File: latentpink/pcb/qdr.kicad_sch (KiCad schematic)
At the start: 69 parts, among them U2 XC7K160T-2FBG484C, U28 IS25WP256D-JLLE, U29 DSC1123CI2-150.0000T, U3 CY7C2245KV18-450BZXI

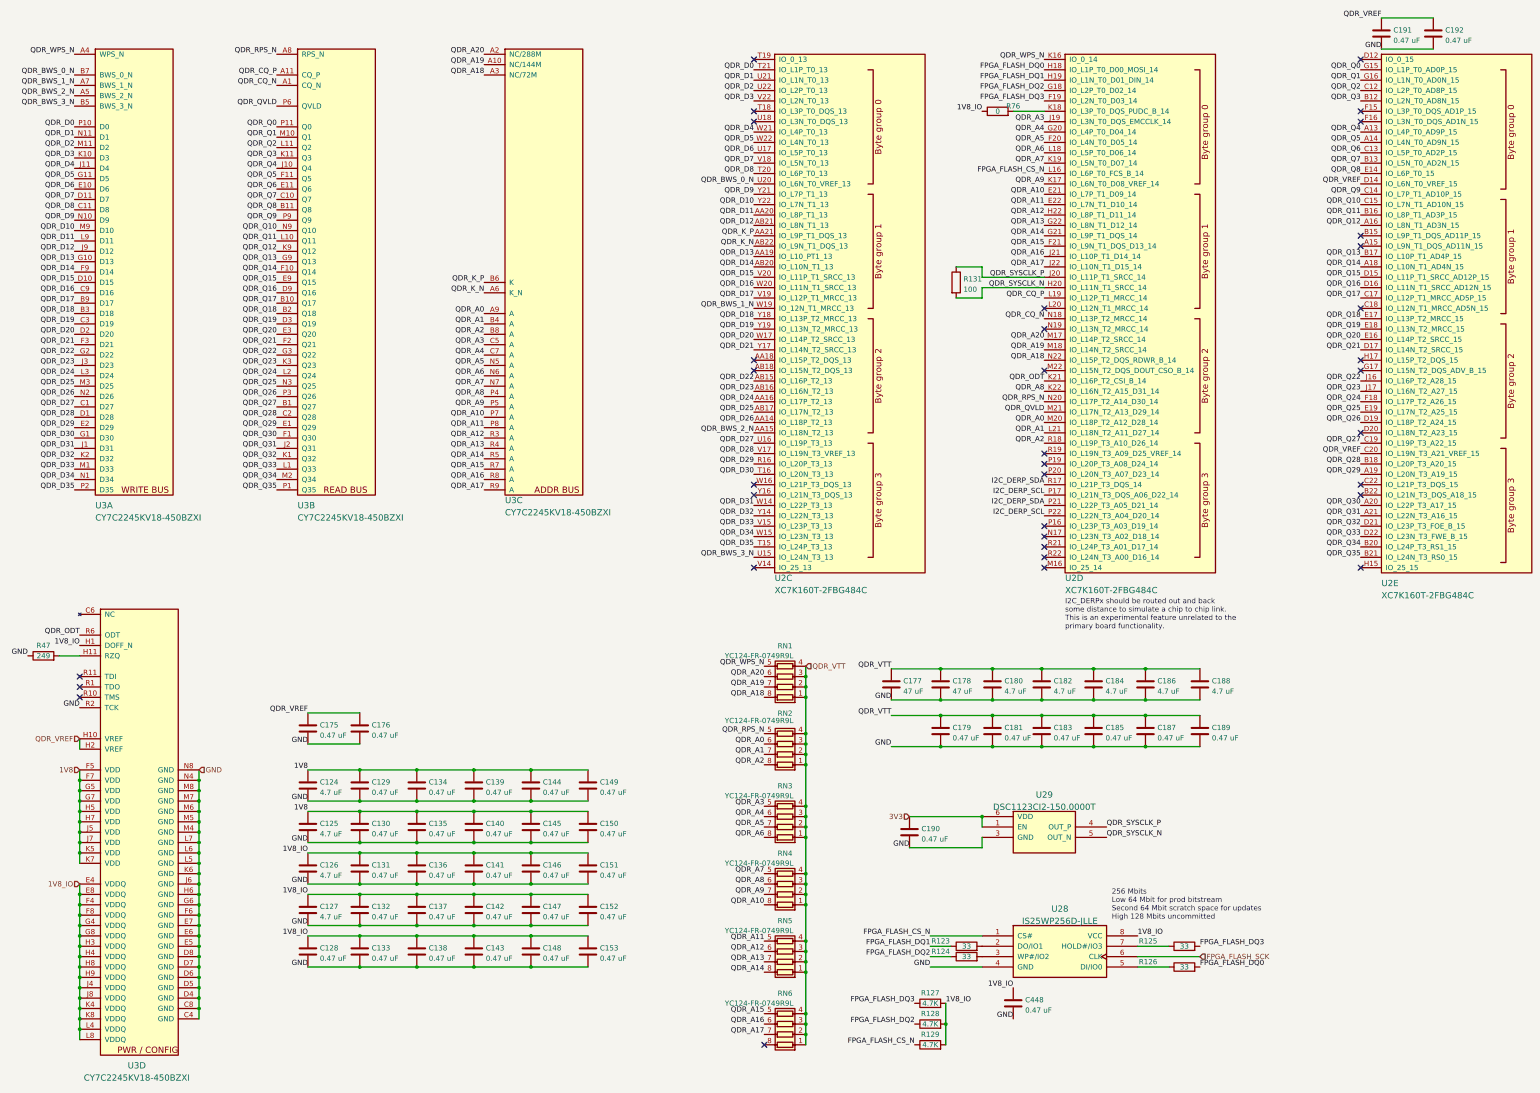
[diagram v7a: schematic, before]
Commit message: Began QDR layout
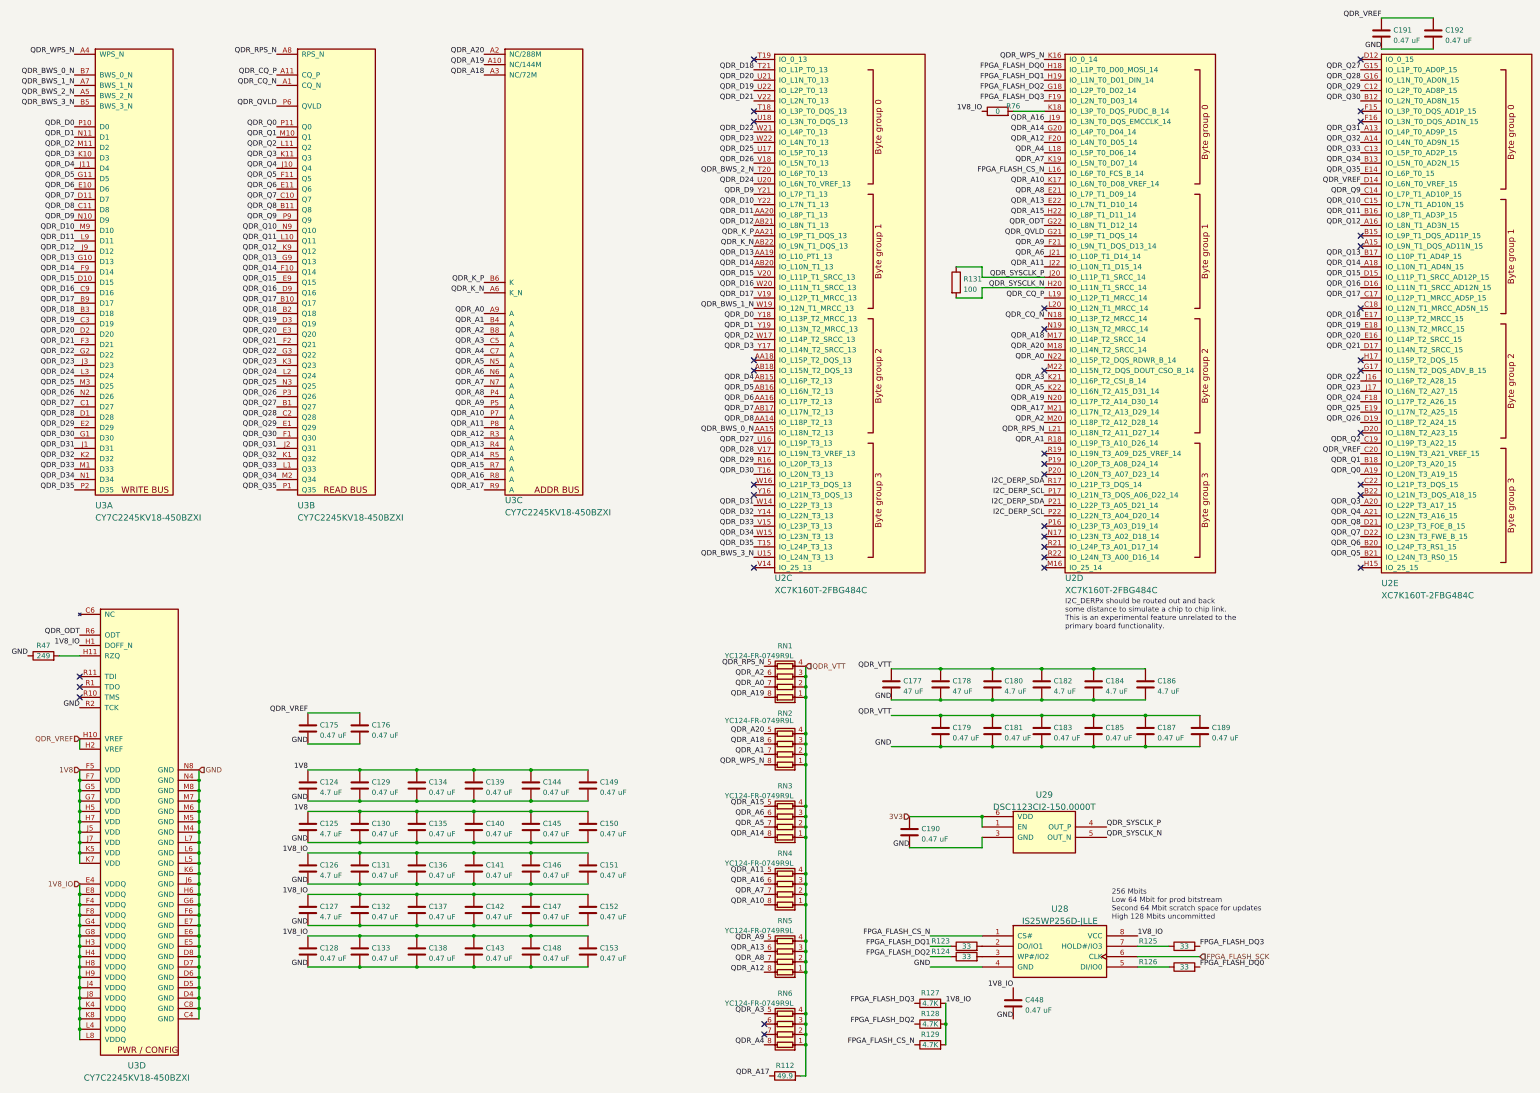
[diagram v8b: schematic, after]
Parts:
- removed C188: 4.7 uF, azonenberg_pcb:EIA_0603_CAP_NOSILK, symbol device:C
- added R112: 49.9, azonenberg_pcb:EIA_0402_RES_NOSILK, symbol device:R
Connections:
- net QDR_A0: now also RN1.7 (R2.2), U2.N22 (IO_L15P_T2_DQS_RDWR_B_14); no longer RN2.6 (R3.2), U2.M20 (IO_L18P_T2_A12_D28_14)
- net QDR_A1: now also U2.R18 (IO_L19P_T3_A10_D26_14); no longer U2.L21 (IO_L18N_T2_A11_D27_14)
- net QDR_A10: now also U2.K17 (IO_L6N_T0_D08_VREF_14); no longer U2.E21 (IO_L7P_T1_D09_14)
- net QDR_A11: now also RN4.5 (R4.2), U2.J22 (IO_L10N_T1_D15_14); no longer RN5.5 (R4.2), U2.E22 (IO_L7N_T1_D10_14)
- net QDR_A12: now also RN5.8 (R1.2), U2.F20 (IO_L4N_T0_D05_14); no longer RN5.6 (R3.2), U2.H22 (IO_L8P_T1_D11_14)
- net QDR_A13: now also RN5.6 (R3.2), U2.E22 (IO_L7N_T1_D10_14); no longer RN5.7 (R2.2), U2.G22 (IO_L8N_T1_D12_14)
- net QDR_A14: now also RN3.8 (R1.2), U2.G20 (IO_L4P_T0_D04_14); no longer RN5.8 (R1.2), U2.G21 (IO_L9P_T1_DQS_14)
- net QDR_A15: now also RN3.5 (R4.2), U2.H22 (IO_L8P_T1_D11_14); no longer RN6.5 (R4.2), U2.F21 (IO_L9N_T1_DQS_D13_14)
- net QDR_A16: now also RN4.6 (R3.2), U2.J19 (IO_L3N_T0_DQS_EMCCLK_14); no longer RN6.6 (R3.2), U2.J21 (IO_L10P_T1_D14_14)
- net QDR_A17: now also U2.M21 (IO_L17N_T2_A13_D29_14), R112.1; no longer RN6.7 (R2.2), U2.J22 (IO_L10N_T1_D15_14)
- net QDR_A18: now also RN2.6 (R3.2), U2.M17 (IO_L14P_T2_SRCC_14); no longer RN1.8 (R1.2), U2.N22 (IO_L15P_T2_DQS_RDWR_B_14)
- net QDR_A19: now also RN1.8 (R1.2), U2.N20 (IO_L17P_T2_A14_D30_14); no longer RN1.7 (R2.2), U2.M18 (IO_L14N_T2_SRCC_14)
- net QDR_A2: now also RN1.6 (R3.2), U2.M20 (IO_L18P_T2_A12_D28_14); no longer RN2.8 (R1.2), U2.R18 (IO_L19P_T3_A10_D26_14)
- net QDR_A20: now also RN2.5 (R4.2), U2.M18 (IO_L14N_T2_SRCC_14); no longer RN1.6 (R3.2), U2.M17 (IO_L14P_T2_SRCC_14)
- net QDR_A3: now also RN6.5 (R4.2), U2.K21 (IO_L16P_T2_CSI_B_14); no longer RN3.5 (R4.2), U2.J19 (IO_L3N_T0_DQS_EMCCLK_14)
- net QDR_A4: now also RN6.8 (R1.2), U2.L18 (IO_L5P_T0_D06_14); no longer RN3.6 (R3.2), U2.G20 (IO_L4P_T0_D04_14)
- net QDR_A5: now also U2.K22 (IO_L16N_T2_A15_D31_14); no longer U2.F20 (IO_L4N_T0_D05_14)
- net QDR_A6: now also RN3.6 (R3.2), U2.J21 (IO_L10P_T1_D14_14); no longer RN3.8 (R1.2), U2.L18 (IO_L5P_T0_D06_14)
- net QDR_A7: now also RN4.7 (R2.2); no longer RN4.5 (R4.2)
- net QDR_A8: now also RN5.7 (R2.2), U2.E21 (IO_L7P_T1_D09_14); no longer RN4.6 (R3.2), U2.K22 (IO_L16N_T2_A15_D31_14)
- net QDR_A9: now also RN5.5 (R4.2), U2.F21 (IO_L9N_T1_DQS_D13_14); no longer RN4.7 (R2.2), U2.K17 (IO_L6N_T0_D08_VREF_14)
- net QDR_BWS_0_N: now also U2.AA15 (IO_L18N_T2_13); no longer U2.U20 (IO_L6N_T0_VREF_13)
- net QDR_BWS_2_N: now also U2.T20 (IO_L6P_T0_13); no longer U2.AA15 (IO_L18N_T2_13)
- net QDR_D0: now also U2.Y18 (IO_L13P_T2_MRCC_13); no longer U2.T21 (IO_L1P_T0_13)
- net QDR_D1: now also U2.Y19 (IO_L13N_T2_MRCC_13); no longer U2.U21 (IO_L1N_T0_13)
- net QDR_D18: now also U2.T21 (IO_L1P_T0_13); no longer U2.Y18 (IO_L13P_T2_MRCC_13)
- net QDR_D19: now also U2.U22 (IO_L2P_T0_13); no longer U2.Y19 (IO_L13N_T2_MRCC_13)
- net QDR_D2: now also U2.W17 (IO_L14P_T2_SRCC_13); no longer U2.U22 (IO_L2P_T0_13)
- net QDR_D20: now also U2.U21 (IO_L1N_T0_13); no longer U2.W17 (IO_L14P_T2_SRCC_13)
- net QDR_D21: now also U2.V22 (IO_L2N_T0_13); no longer U2.Y17 (IO_L14N_T2_SRCC_13)
- net QDR_D22: now also U2.W21 (IO_L4P_T0_13); no longer U2.AB15 (IO_L16P_T2_13)
- net QDR_D23: now also U2.W22 (IO_L4N_T0_13); no longer U2.AB16 (IO_L16N_T2_13)
- net QDR_D24: now also U2.U20 (IO_L6N_T0_VREF_13); no longer U2.AA16 (IO_L17P_T2_13)
- net QDR_D25: now also U2.U17 (IO_L5P_T0_13); no longer U2.AB17 (IO_L17N_T2_13)
- net QDR_D26: now also U2.V18 (IO_L5N_T0_13); no longer U2.AA14 (IO_L18P_T2_13)
- net QDR_D3: now also U2.Y17 (IO_L14N_T2_SRCC_13); no longer U2.V22 (IO_L2N_T0_13)
- net QDR_D4: now also U2.AB15 (IO_L16P_T2_13); no longer U2.W21 (IO_L4P_T0_13)
- net QDR_D5: now also U2.AB16 (IO_L16N_T2_13); no longer U2.W22 (IO_L4N_T0_13)
- net QDR_D6: now also U2.AA16 (IO_L17P_T2_13); no longer U2.U17 (IO_L5P_T0_13)
- net QDR_D7: now also U2.AB17 (IO_L17N_T2_13); no longer U2.V18 (IO_L5N_T0_13)
- net QDR_D8: now also U2.AA14 (IO_L18P_T2_13); no longer U2.T20 (IO_L6P_T0_13)
- net QDR_ODT: now also U2.G22 (IO_L8N_T1_D12_14); no longer U2.K21 (IO_L16P_T2_CSI_B_14)
- net QDR_Q0: now also U2.A19 (IO_L20N_T3_A19_15); no longer U2.G15 (IO_L1P_T0_AD0P_15)
- net QDR_Q1: now also U2.B18 (IO_L20P_T3_A20_15); no longer U2.G16 (IO_L1N_T0_AD0N_15)
- net QDR_Q2: now also U2.C19 (IO_L19P_T3_A22_15); no longer U2.C12 (IO_L2P_T0_AD8P_15)
- net QDR_Q27: now also U2.G15 (IO_L1P_T0_AD0P_15); no longer U2.C19 (IO_L19P_T3_A22_15)
- net QDR_Q28: now also U2.G16 (IO_L1N_T0_AD0N_15); no longer U2.B18 (IO_L20P_T3_A20_15)
- net QDR_Q29: now also U2.C12 (IO_L2P_T0_AD8P_15); no longer U2.A19 (IO_L20N_T3_A19_15)
- net QDR_Q3: now also U2.A20 (IO_L22P_T3_A17_15); no longer U2.B12 (IO_L2N_T0_AD8N_15)
- net QDR_Q30: now also U2.B12 (IO_L2N_T0_AD8N_15); no longer U2.A20 (IO_L22P_T3_A17_15)
- net QDR_Q31: now also U2.A13 (IO_L4P_T0_AD9P_15); no longer U2.A21 (IO_L22N_T3_A16_15)
- net QDR_Q32: now also U2.A14 (IO_L4N_T0_AD9N_15); no longer U2.D21 (IO_L23P_T3_FOE_B_15)
- net QDR_Q33: now also U2.C13 (IO_L5P_T0_AD2P_15); no longer U2.D22 (IO_L23N_T3_FWE_B_15)
- net QDR_Q34: now also U2.B13 (IO_L5N_T0_AD2N_15); no longer U2.B20 (IO_L24P_T3_RS1_15)
- net QDR_Q35: now also U2.E14 (IO_L6P_T0_15); no longer U2.B21 (IO_L24N_T3_RS0_15)
- net QDR_Q4: now also U2.A21 (IO_L22N_T3_A16_15); no longer U2.A13 (IO_L4P_T0_AD9P_15)
- net QDR_Q5: now also U2.B21 (IO_L24N_T3_RS0_15); no longer U2.A14 (IO_L4N_T0_AD9N_15)
- net QDR_Q6: now also U2.B20 (IO_L24P_T3_RS1_15); no longer U2.C13 (IO_L5P_T0_AD2P_15)
- net QDR_Q7: now also U2.D22 (IO_L23N_T3_FWE_B_15); no longer U2.B13 (IO_L5N_T0_AD2N_15)
- net QDR_Q8: now also U2.D21 (IO_L23P_T3_FOE_B_15); no longer U2.E14 (IO_L6P_T0_15)
- net QDR_QVLD: now also U2.G21 (IO_L9P_T1_DQS_14); no longer U2.M21 (IO_L17N_T2_A13_D29_14)
- net QDR_RPS_N: now also RN1.5 (R4.2), U2.L21 (IO_L18N_T2_A11_D27_14); no longer RN2.5 (R4.2), U2.N20 (IO_L17P_T2_A14_D30_14)
- net QDR_VTT: now also R112.2
- net QDR_WPS_N: now also RN2.8 (R1.2); no longer RN1.5 (R4.2)
- no-connect marks 35 -> 36
